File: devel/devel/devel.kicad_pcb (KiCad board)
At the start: 2 copper layers, 64 parts, among them SW1 SW, SW10 SW, SW11 SW, SW12 SW, SW13 SW, SW14 SW, SW15 SW, SW2 SW, SW3 SW, SW4 SW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

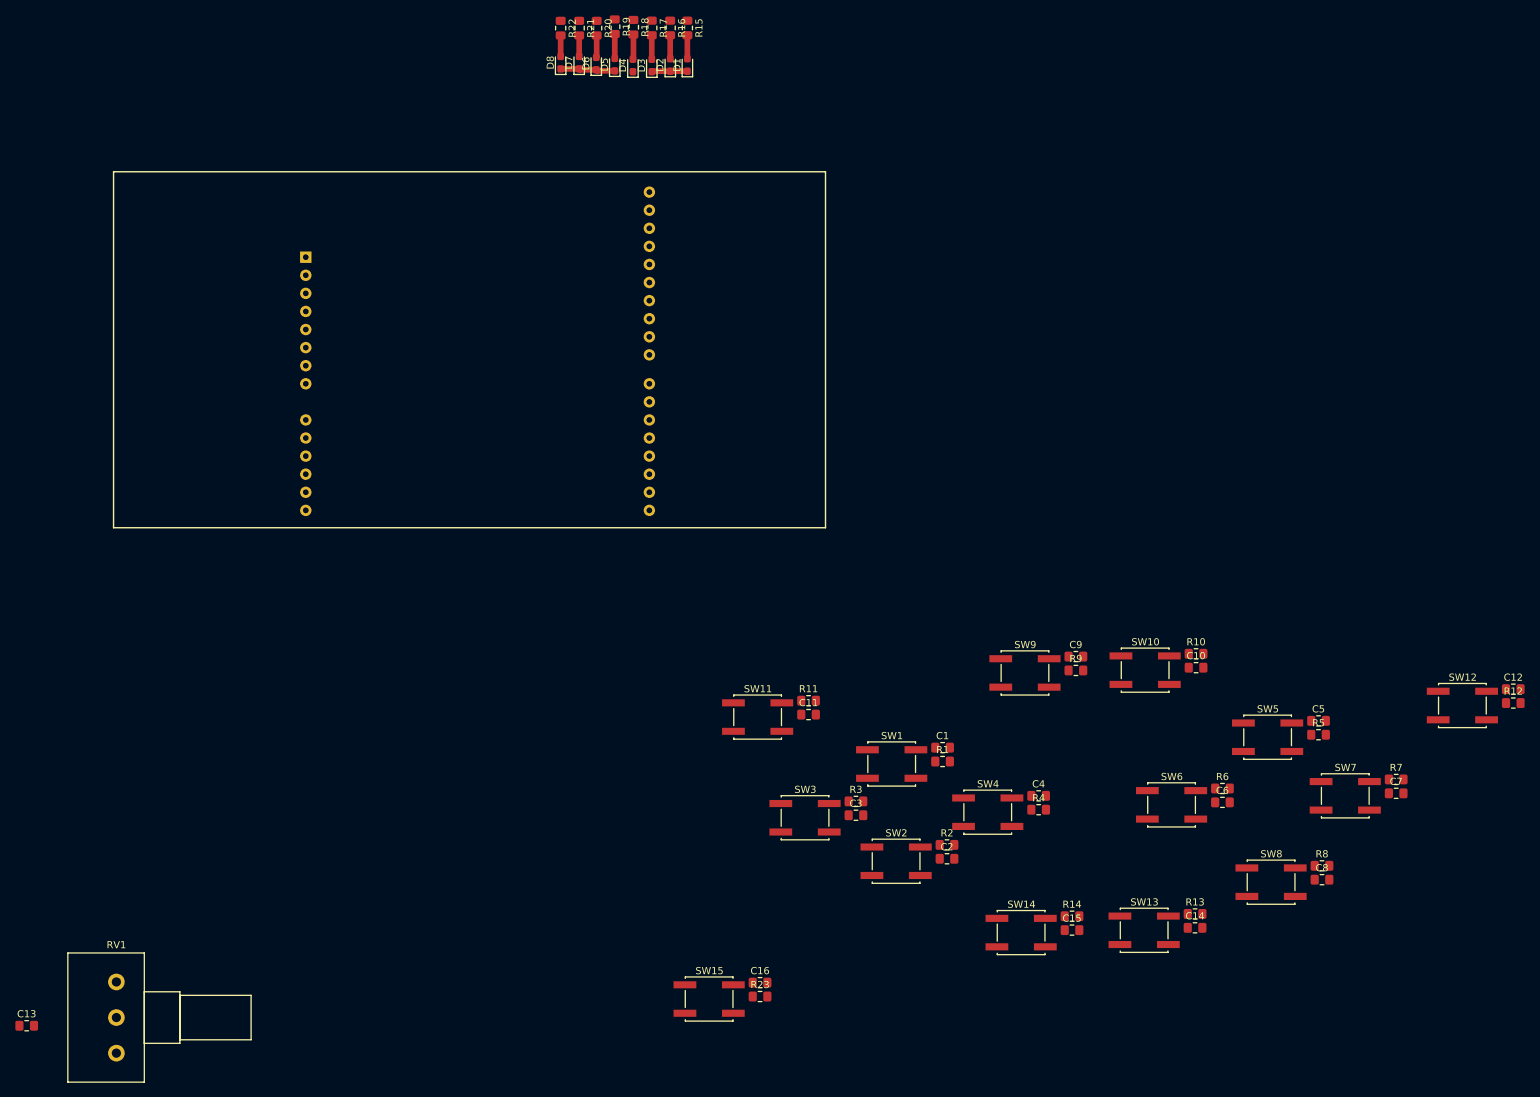
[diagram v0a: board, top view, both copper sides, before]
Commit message: Preliminary placement and orientation of components to fit the board
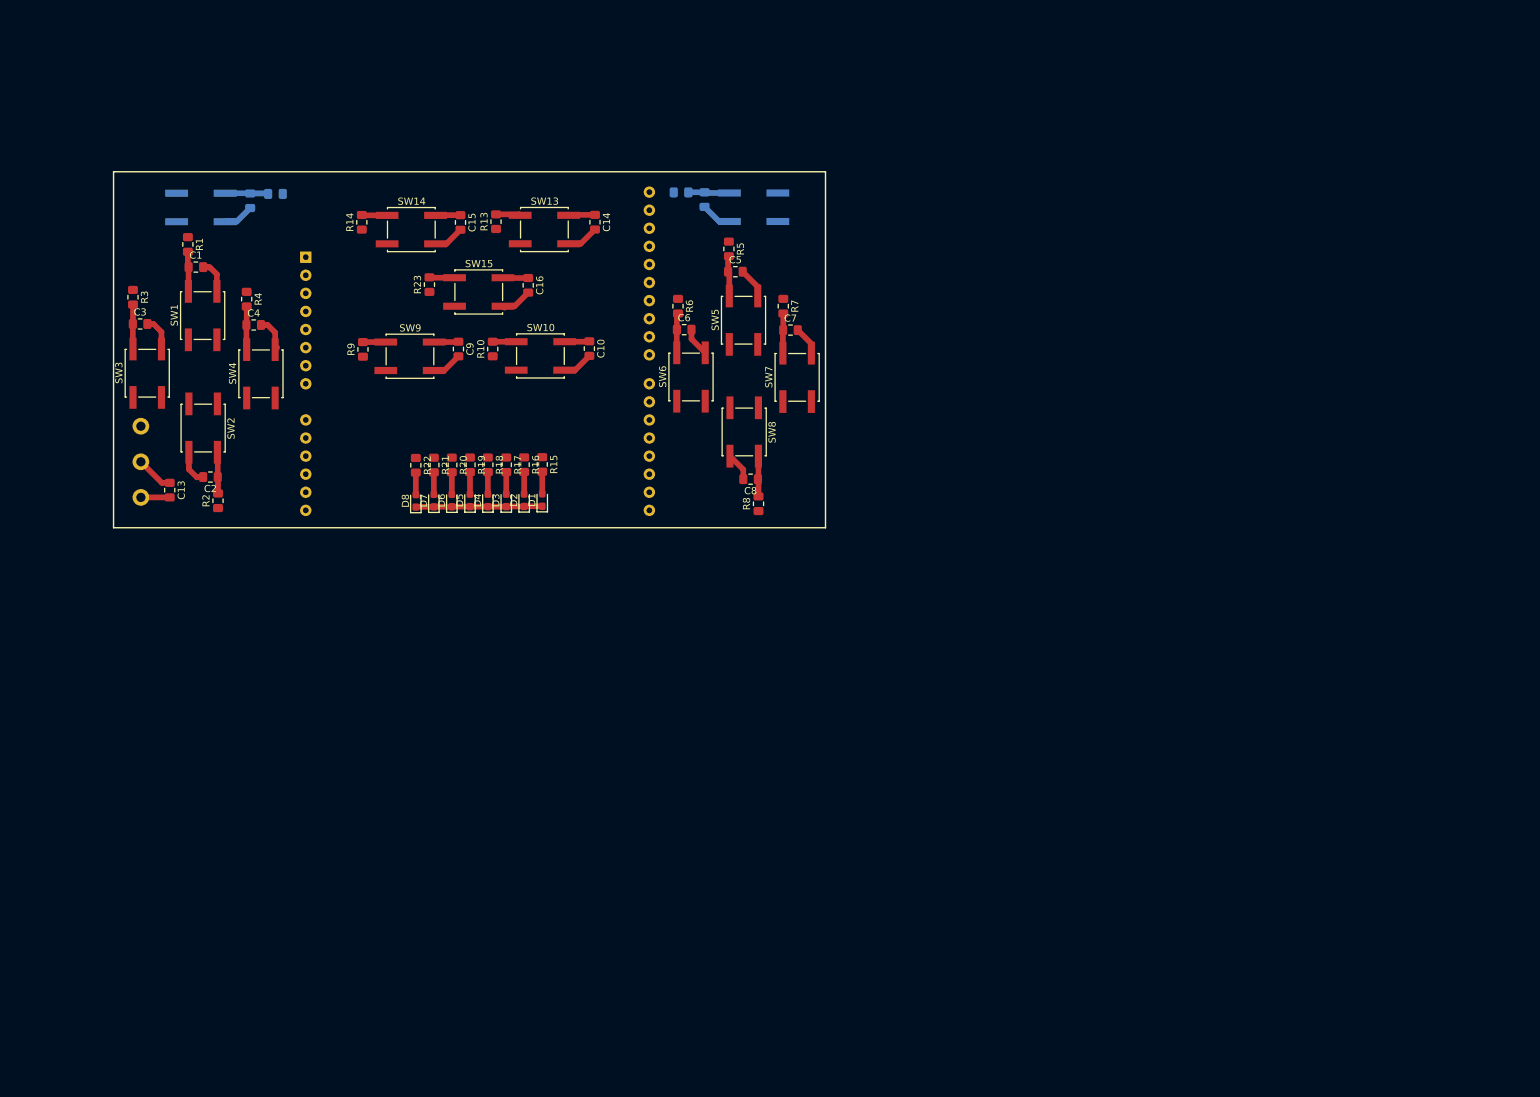
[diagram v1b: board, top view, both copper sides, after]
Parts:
- C11, C12, R11, R12, RV1, SW11, SW12: moved to B.Cu
- moved R14 139.5 mm to (74.9, 47.1), turned to 90 degrees
- moved R13 138.2 mm to (93.7, 47.0), turned to 90 degrees
- moved R12 137.1 mm to (119.7, 42.9)
- moved C12 132.8 mm to (123.0, 43.9), turned to 270 degrees
- moved R4 132.3 mm to (58.7, 57.9), turned to 270 degrees
- moved C15 131.4 mm to (88.7, 47.1), turned to 270 degrees
- moved SW14 130.7 mm to (81.8, 48.1)
- moved C14 130.1 mm to (107.6, 47.1), turned to 270 degrees
- moved SW13 129.6 mm to (100.5, 48.1)
- moved C4 128.6 mm to (59.7, 61.5)
- moved R1 128.5 mm to (50.4, 50.2), turned to 270 degrees
- moved C1 124.7 mm to (51.6, 53.4)
- moved R3 123.8 mm to (42.7, 57.6), turned to 270 degrees
- moved C3 121.9 mm to (43.7, 61.4)
- moved SW12 121.7 mm to (129.9, 45.0), turned to 180 degrees
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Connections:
- A1 pad 1: (no net) -> Net-(A1-Pad1)
- A1 pad 2: (no net) -> Net-(A1-Pad2)
- A1 pad 8: (no net) -> Net-(A1-Pad8)
- C1 pad 1: /P0.19 -> /P0.02
- C2 pad 1: /P0.20 -> /P0.29
- C3 pad 1: /P0.22 -> /P0.04
- C4 pad 1: /P0.23 -> /P0.28
- C5 pad 1: /P0.02 -> /P0.19
- C6 pad 1: /P0.04 -> /P0.22
- C7 pad 1: /P0.28 -> /P0.23
- C8 pad 1: /P0.29 -> /P0.20
- R1 pad 1: /5V -> /VDD
- R1 pad 2: /P0.19 -> /P0.02
- R11 pad 1: /5V -> /VDD
- R13 pad 1: /5V -> /VDD
- R2 pad 2: /P0.20 -> /P0.29
- R3 pad 1: /5V -> /VDD
- R3 pad 2: /P0.22 -> /P0.04
- R4 pad 2: /P0.23 -> /P0.28
- R5 pad 1: /5V -> /VDD
- R5 pad 2: /P0.02 -> /P0.19
- R6 pad 2: /P0.04 -> /P0.22
- R7 pad 1: /5V -> /VDD
- R7 pad 2: /P0.28 -> /P0.23
- R8 pad 2: /P0.29 -> /P0.20
- R9 pad 1: /5V -> /VDD
- SW1 pad 1: /P0.19 -> /P0.02
- SW2 pad 1: /P0.20 -> /P0.29
- SW3 pad 1: /P0.22 -> /P0.04
- SW4 pad 1: /P0.23 -> /P0.28
- SW5 pad 1: /P0.02 -> /P0.19
- SW6 pad 1: /P0.04 -> /P0.22
- SW7 pad 1: /P0.28 -> /P0.23
- SW8 pad 1: /P0.29 -> /P0.20
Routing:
- net /GND: track 12.9 -> 89.9 mm
- net /P0.27: track 0.00 -> 7.28 mm
- net /P0.26: track 0.00 -> 7.27 mm
- net /P0.28: track 0.00 -> 7.19 mm
- net /RESET: track 0.00 -> 7.11 mm
- net /P0.30: track 0.00 -> 6.88 mm
- net /P0.23: track 0.00 -> 6.70 mm
- net /P0.24: track 0.00 -> 6.63 mm
- net /P0.04: track 0.00 -> 6.27 mm
- net /P0.25: track 0.00 -> 6.09 mm
- net /P0.31: track 0.00 -> 5.82 mm
- net /P0.29: track 0.00 -> 5.82 mm
- net /P0.20: track 0.00 -> 5.72 mm
- net /P0.19: track 0.00 -> 5.70 mm
- net /P0.02: track 0.00 -> 5.62 mm
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
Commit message: Made Gustav's design into a double sided board
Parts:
- moved R6 20.3 mm to (122.8, 78.9), turned to 90 degrees
- moved C6 13.6 mm to (121.9, 75.6), turned to 180 degrees
- moved R11 1.16 mm to (62.0, 44.0), turned to 90 degrees
- moved R12 1.14 mm to (120.0, 44.0), turned to 90 degrees
- moved SW6 0.22 mm to (120.9, 69.0), turned to 270 degrees
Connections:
- A1 pad 1: Net-(A1-Pad1) -> (no net)
- A1 pad 2: Net-(A1-Pad2) -> (no net)
- A1 pad 5: /5V -> (no net)
- A1 pad 8: Net-(A1-Pad8) -> (no net)
- C1 pad 1: /P0.02 -> /P0.29
- C10 pad 1: /P0.30 -> /P0.25
- C11 pad 1: /P0.25 -> /P0.04
- C12 pad 1: /P0.31 -> /P0.02
- C2 pad 1: /P0.29 -> /P0.31
- C3 pad 1: /P0.04 -> /P0.30
- C5 pad 1: /P0.19 -> /P0.23
- C7 pad 1: /P0.23 -> /P0.20
- C8 pad 1: /P0.20 -> /P0.19
- R1 pad 2: /P0.02 -> /P0.29
- R10 pad 2: /P0.30 -> /P0.25
- R11 pad 2: /P0.25 -> /P0.04
- R12 pad 2: /P0.31 -> /P0.02
- R2 pad 2: /P0.29 -> /P0.31
- R3 pad 2: /P0.04 -> /P0.30
- R5 pad 2: /P0.19 -> /P0.23
- R7 pad 2: /P0.23 -> /P0.20
- R8 pad 2: /P0.20 -> /P0.19
- SW1 pad 1: /P0.02 -> /P0.29
- SW10 pad 1: /P0.30 -> /P0.25
- SW11 pad 1: /P0.25 -> /P0.04
- SW12 pad 1: /P0.31 -> /P0.02
- SW2 pad 1: /P0.29 -> /P0.31
- SW3 pad 1: /P0.04 -> /P0.30
- SW5 pad 1: /P0.19 -> /P0.23
- SW7 pad 1: /P0.23 -> /P0.20
- SW8 pad 1: /P0.20 -> /P0.19
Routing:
- net /VDD: track 0.00 -> 294.7 mm, vias 0 -> 2
- net /P0.04: track 6.27 -> 57.3 mm, vias 0 -> 1
- net /P0.03(A0): track 5.28 -> 54.5 mm
- net /P0.24: track 6.63 -> 51.2 mm
- net /P0.30: track 6.88 -> 48.1 mm
- net /P0.02: track 5.62 -> 43.0 mm, vias 0 -> 1
- net /P0.18: track 0.02 -> 37.1 mm
- net /P0.29: track 5.82 -> 41.7 mm
- net /P0.27: track 7.28 -> 41.8 mm
- net /P0.17: track 0.00 -> 33.5 mm
- net /P0.16: track 0.00 -> 30.9 mm
- net /P0.20: track 5.72 -> 35.3 mm
- net /P0.15: track 0.00 -> 28.4 mm
- net /P0.19: track 5.70 -> 33.3 mm
- net /P0.14: track 0.00 -> 25.9 mm
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- added copper zone on B.Cu, net /GND
- added copper zone on F.Cu, net /GND
